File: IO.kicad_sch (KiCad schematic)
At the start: 16 parts

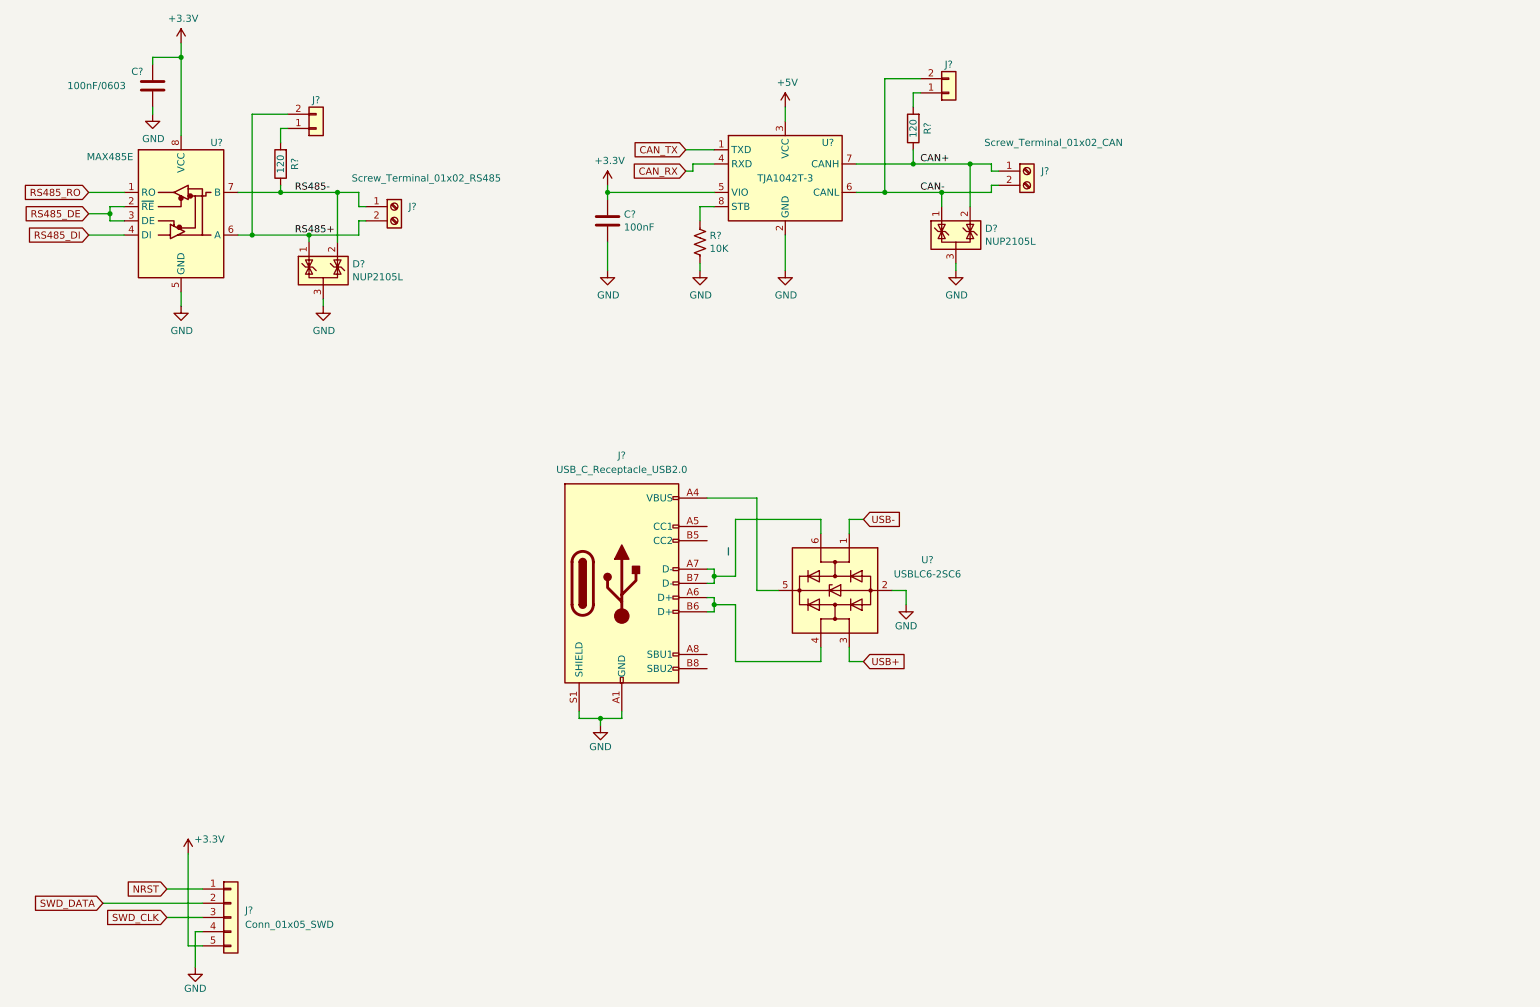
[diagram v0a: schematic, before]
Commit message: add IO, MCU, power sheets
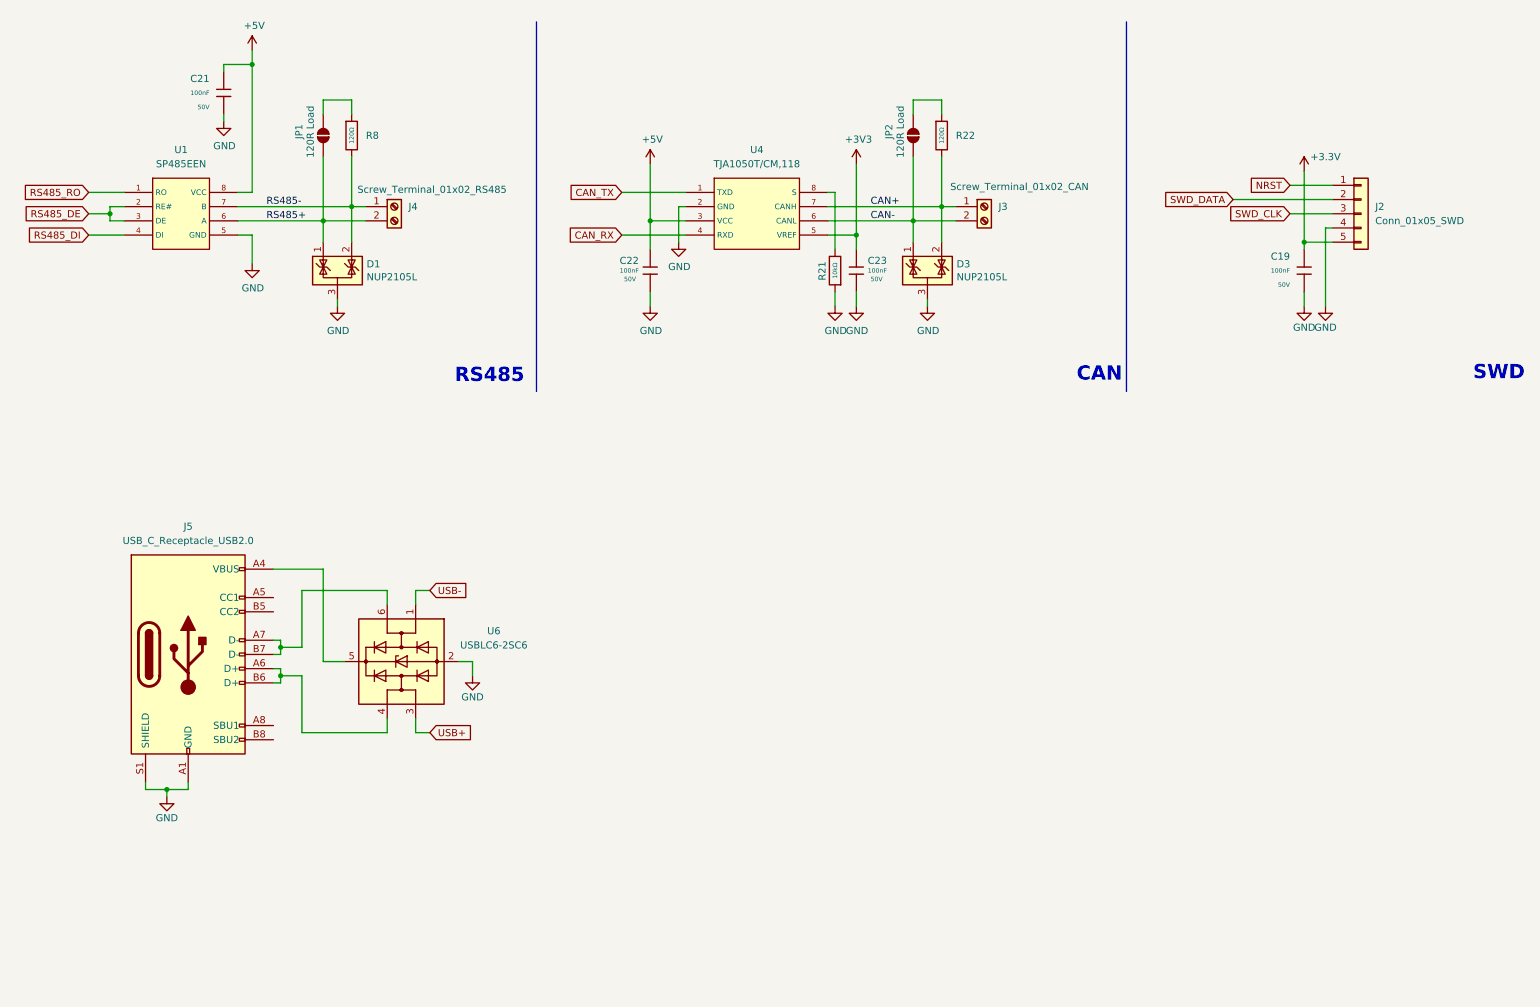
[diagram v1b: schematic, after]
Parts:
- removed C?: 100nF, asemsys_footprint_lib:C_0402, symbol Device:C
- removed C?: 100nF/0603, Capacitor_SMD:C_0603_1608Metric, symbol Device:C
- removed D?: NUP2105L, asemsys_footprint_lib:SOT23-3, symbol Power_Protection:NUP2105L
- removed J?: Screw_Terminal_01x02_CAN, symbol Connector:Screw_Terminal_01x02
- removed J? (x2): ~, symbol Connector_Generic:Conn_01x02
- removed R? (x2): 120, Resistor_SMD:R_0603_1608Metric, symbol Device:R
- removed R?: 10K, asemsys_footprint_lib:R_0402, symbol Device:R_US
- removed U?: TJA1042T-3, asemsys_footprint_lib:SOIC-8, symbol Interface_CAN_LIN:TJA1042T-3
- removed U?: MAX485E, asemsys_footprint_lib:SOIC-8, symbol Interface_UART:MAX485E
- added C19, C21, C22, C23: 100nF, PCM_JLCPCB:C_0603, symbol PCM_JLCPCB-Capacitors:0603,100nF
- added D3: NUP2105L, asemsys_footprint_lib:SOT23-3, symbol Power_Protection:NUP2105L
- added J3: Screw_Terminal_01x02_CAN, symbol Connector:Screw_Terminal_01x02
- added JP1, JP2: 120R Load, symbol Jumper:SolderJumper_2_Open
- added R21: 10kΩ, PCM_JLCPCB:R_0603, symbol PCM_JLCPCB-Resistors:0603,10kΩ
- added R22, R8: 120Ω, PCM_JLCPCB:R_0603, symbol PCM_JLCPCB-Resistors:0603,120Ω
- added U1: SP485EEN, PCM_JLCPCB:SOIC-8_L5.0-W4.0-P1.27-LS6.0-BL, symbol PCM_JLCPCB-Interface:Transceiver, RS485/422, 10Mbps, SP485EEN-L/TR
- added U4: TJA1050T/CM,118, PCM_JLCPCB:SOIC-8_L5.0-W4.0-P1.27-LS6.0-BL, symbol PCM_JLCPCB-Interface:Transceiver, CAN, TJA1050T
- gave numbers to parts that had none: 5
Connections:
- net +3.3V: now also C19.1
- net +3V3: now also C23.1, U4.5 (VREF)
- net +5V: now also C21.1, C22.1, U1.8 (VCC), U4.3 (VCC)
- net CAN+: now also D3.2 (K), J3.1 (Pin_1), R22.2, U4.7 (CANH)
- net CAN-: now also D3.1 (K), J3.2 (Pin_2), JP2.1 (A), U4.6 (CANL)
- net CAN_RX: now also U4.4 (RXD)
- net CAN_TX: now also U4.1 (TXD)
- net GND: now also C19.2, C21.2, C22.2, C23.2, D3.3 (A), R21.1, U1.5 (GND), U4.2 (GND)
- net RS485+: now also JP1.1 (A), U1.6 (A)
- net RS485-: now also R8.2, U1.7 (B)
- net RS485_DE: now also U1.2 (RE#), U1.3 (DE)
- net RS485_DI: now also U1.4 (DI)
- net RS485_RO: now also U1.1 (RO)
- new net: JP1.2 (B), R8.1
- new net: JP2.2 (B), R22.1
- new net: R21.2, U4.8 (S)
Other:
- note added: "CAN"
- note added: "RS485"
- note added: "SWD"
- moved on the sheet: D1, J2, J5, U6

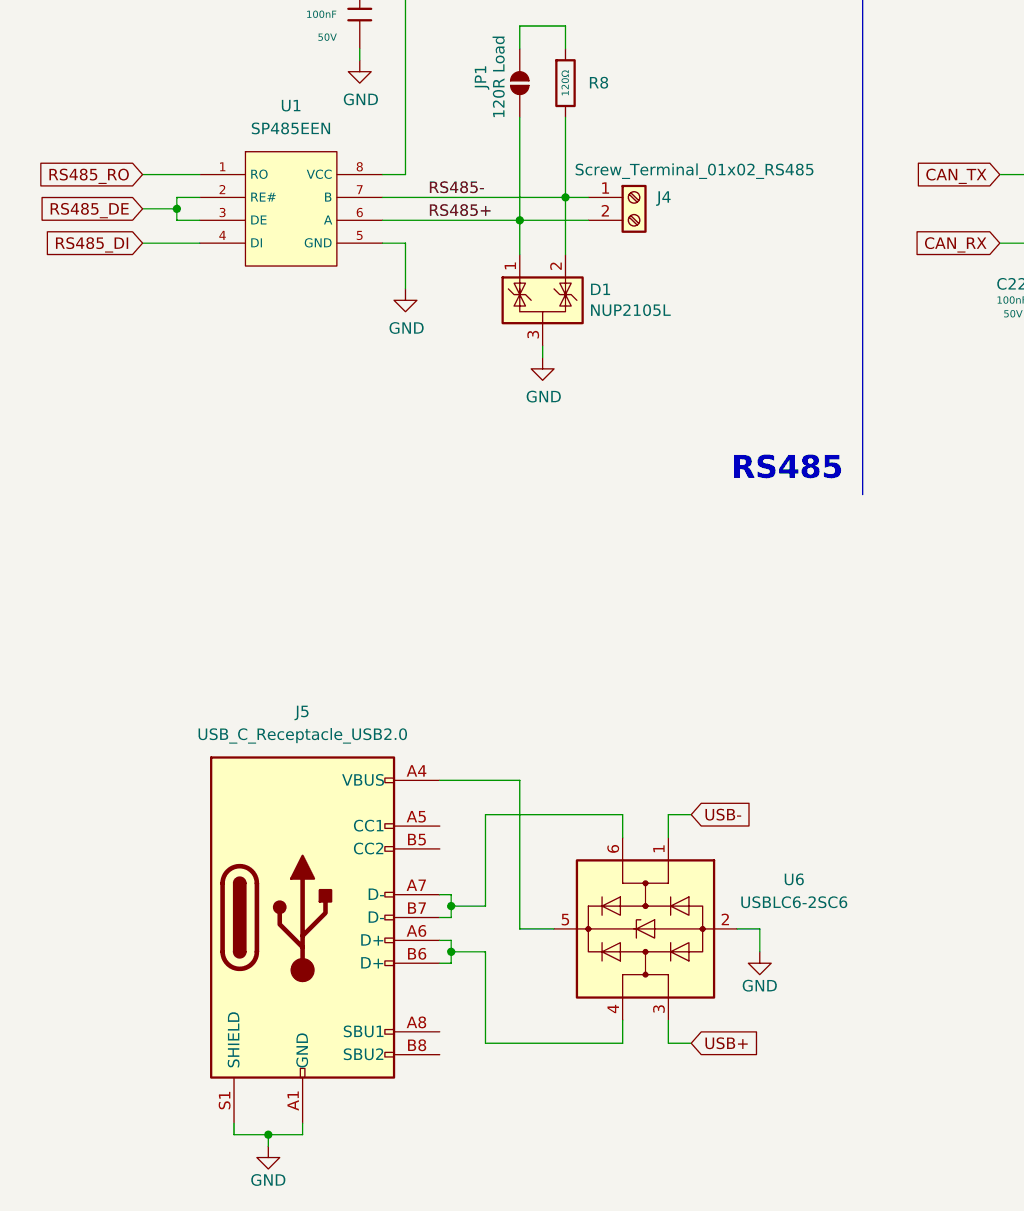
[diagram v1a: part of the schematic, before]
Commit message: Add encoder sheet
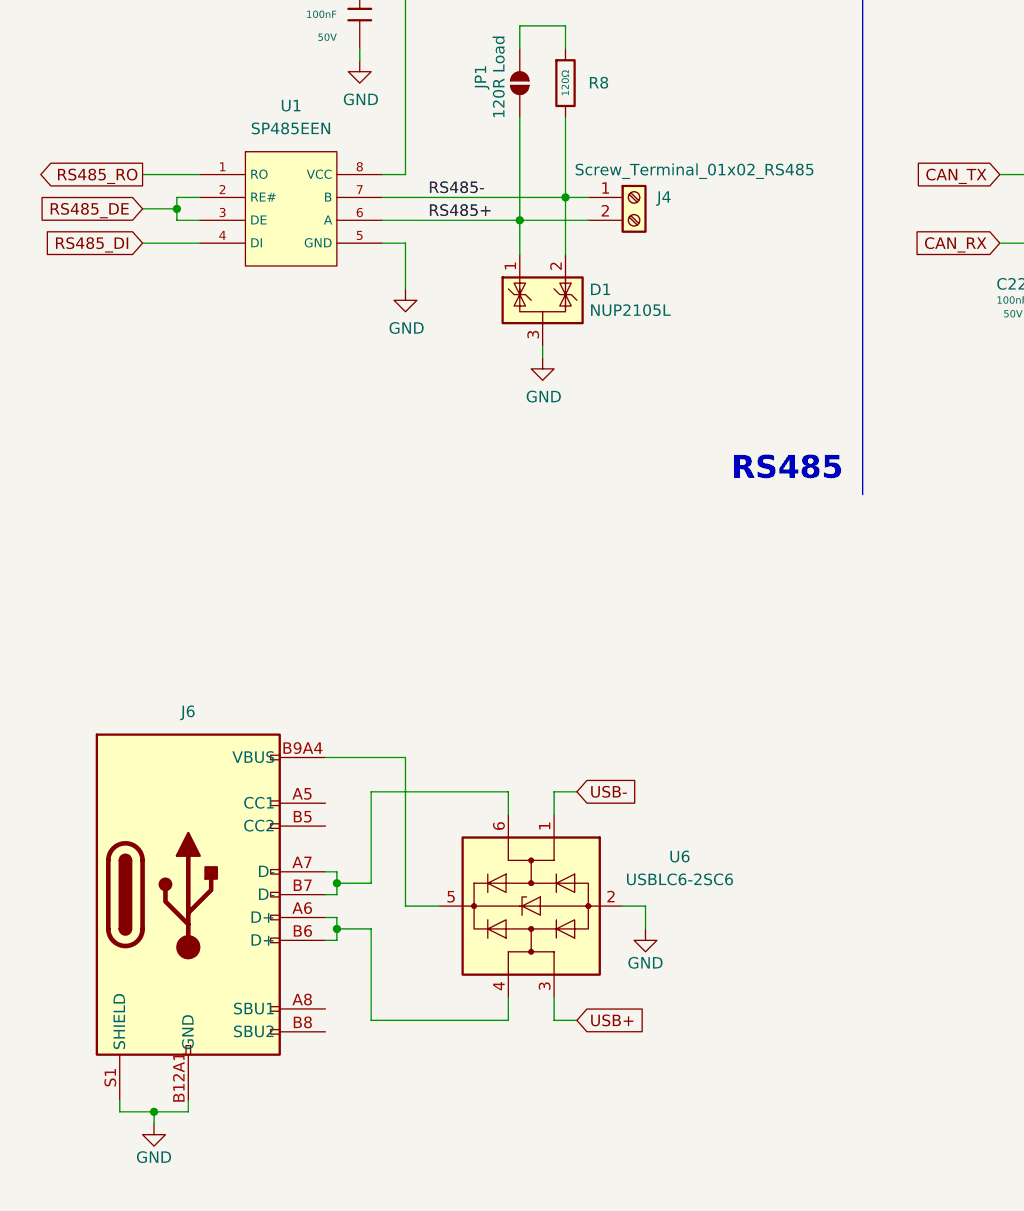
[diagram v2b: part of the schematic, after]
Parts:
- removed J5: USB_C_Receptacle_USB2.0, symbol Connector:USB_C_Receptacle_USB2.0
- added J6: Connector, USB-TYPE-C-16P, PCM_JLCPCB:TYPE-C-SMD_HX-TYPE-C-16PIN, symbol PCM_JLCPCB-Extended:Connector, USB-TYPE-C-16P
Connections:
- net GND: now also J6.A12B1 (GND), J6.B12A1 (GND), J6.S1 (SHIELD)
- net at U6.4 (I/O2): now also J6.A6 (D+), J6.B6 (D+)
- net at U6.5 (VBUS): now also J6.A9B4 (VBUS), J6.B9A4 (VBUS)
- net at U6.6 (I/O1): now also J6.A7 (D-), J6.B7 (D-)
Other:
- moved on the sheet: U6

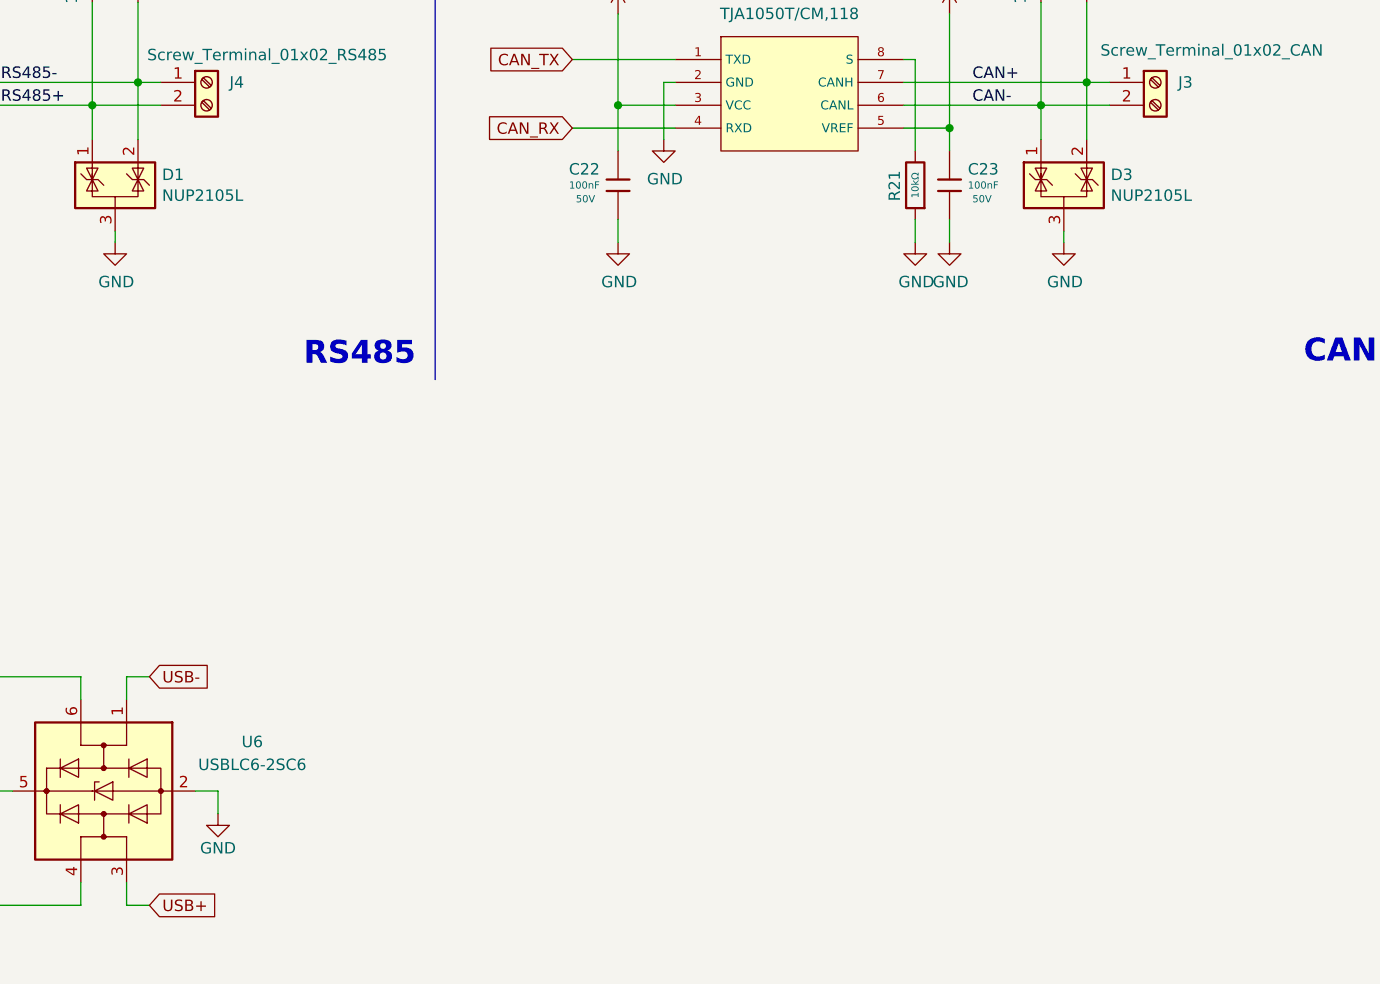
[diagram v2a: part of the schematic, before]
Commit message: Add mcu connections
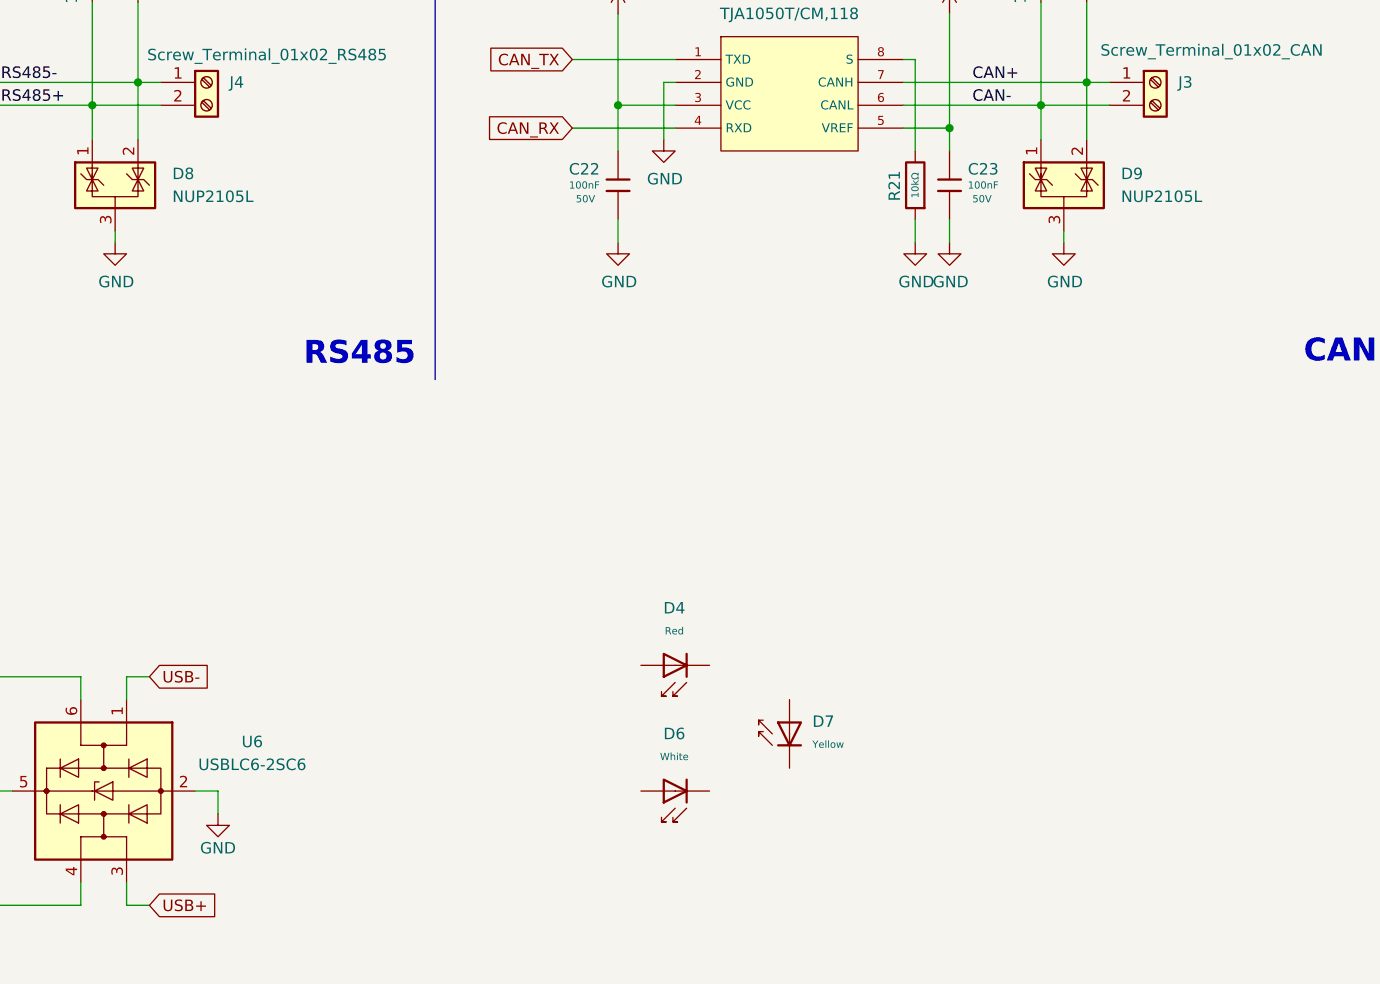
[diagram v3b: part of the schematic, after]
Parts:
- removed D1, D3: NUP2105L, asemsys_footprint_lib:SOT23-3, symbol Power_Protection:NUP2105L
- added D4: Red, PCM_JLCPCB:D_0603, symbol PCM_JLCPCB-Diodes:LED,0603,Red
- added D6: White, PCM_JLCPCB:D_0603, symbol PCM_JLCPCB-Diodes:LED,0603,White
- added D7: Yellow, PCM_JLCPCB:D_0603, symbol PCM_JLCPCB-Diodes:LED,0603,Yellow
- added D8, D9: NUP2105L, Package_TO_SOT_SMD:SOT-23, symbol Power_Protection:NUP2105L
- JP1, JP2: footprint (none) -> Jumper:SolderJumper-2_P1.3mm_Open_TrianglePad1.0x1.5mm
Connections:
- net CAN+: now also D9.2 (K)
- net CAN-: now also D9.1 (K)
- net GND: now also D8.3 (A), D9.3 (A)
- net RS485+: now also D8.1 (K)
- net RS485-: now also D8.2 (K)
